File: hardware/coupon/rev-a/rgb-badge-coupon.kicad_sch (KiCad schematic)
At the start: 0 parts

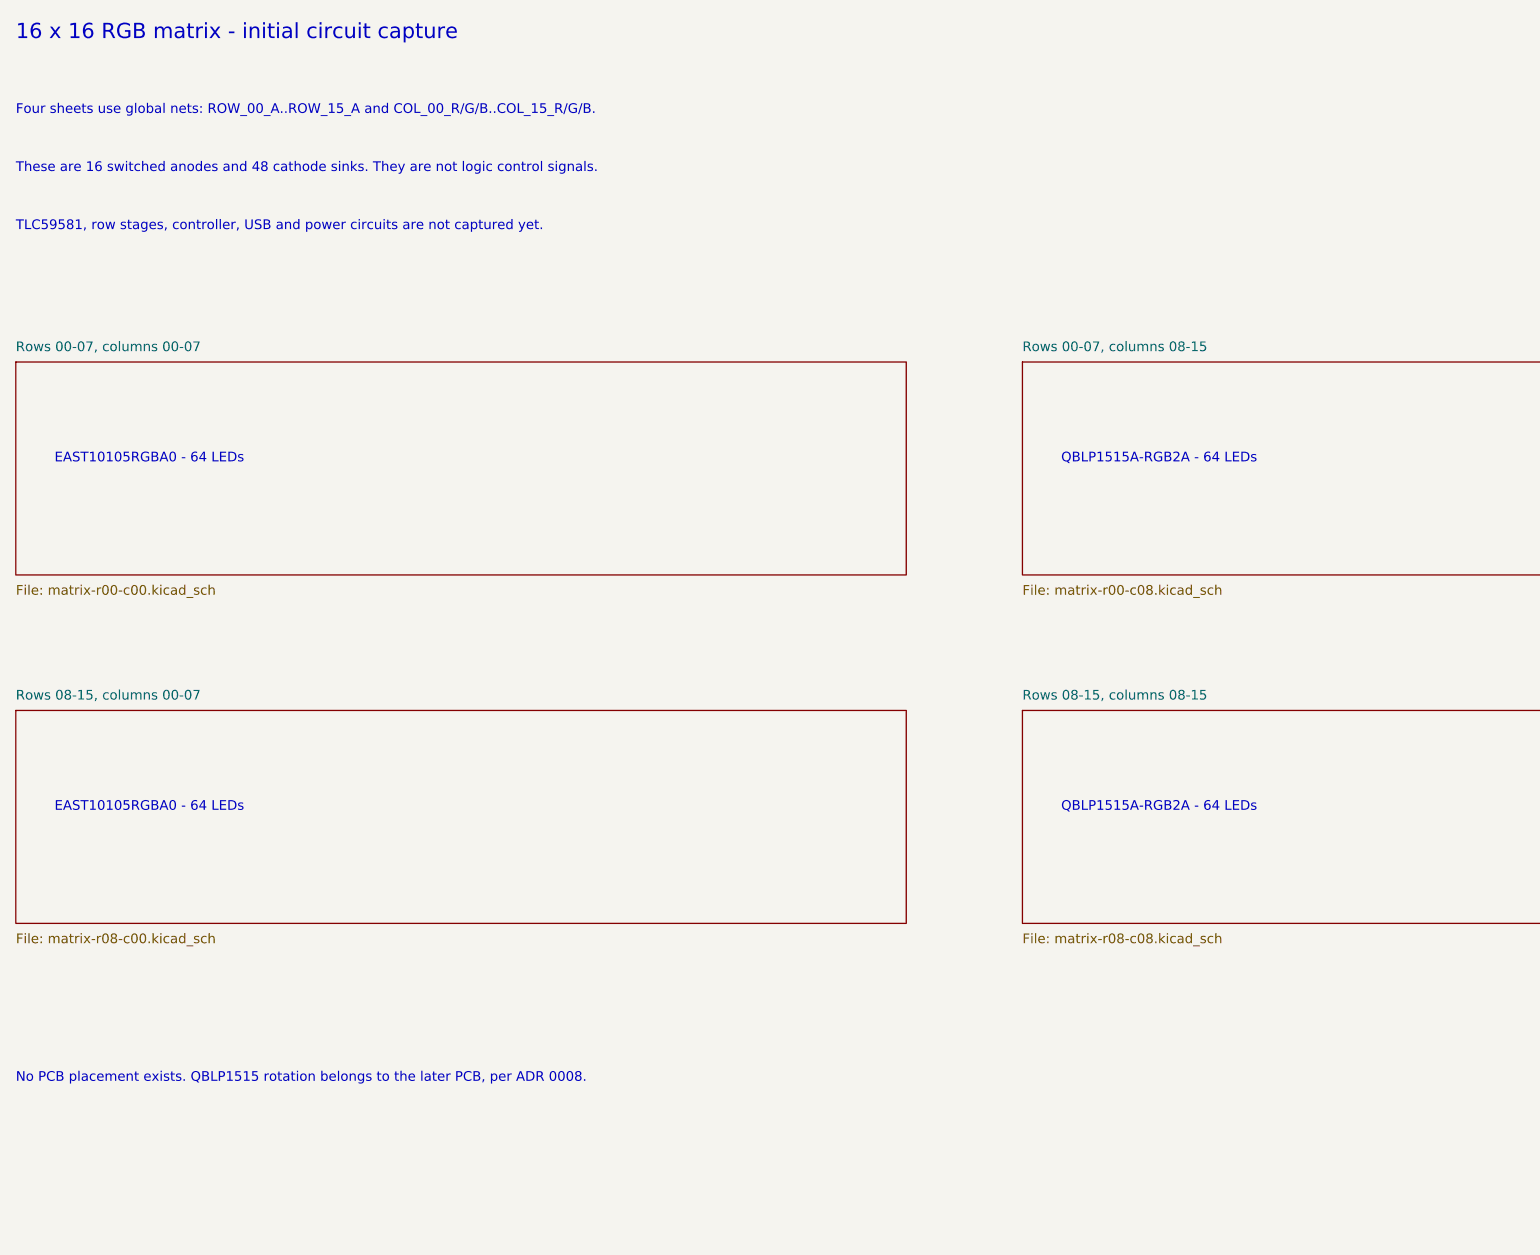
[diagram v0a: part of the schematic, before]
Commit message: Capture TLC59581 coupon driver and audit its current reference and footprint
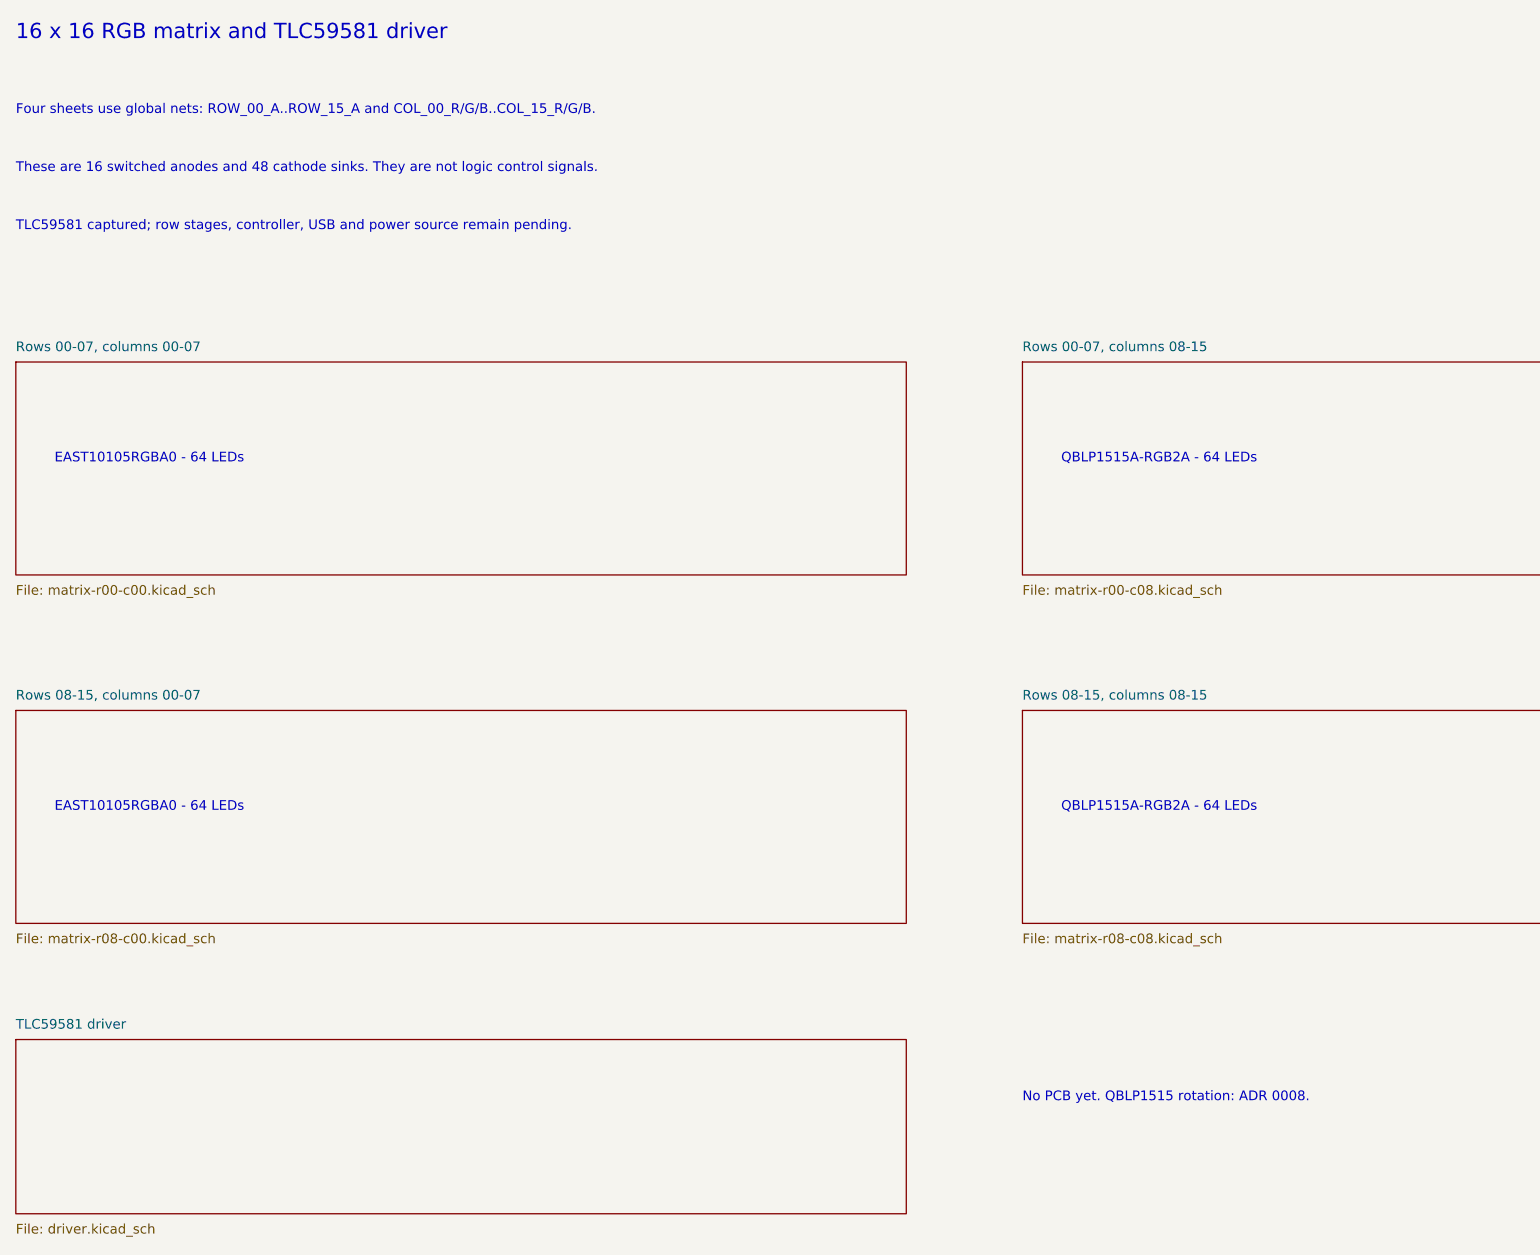
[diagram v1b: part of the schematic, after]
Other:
- added sheet TLC59581 driver (driver.kicad_sch)
- note added: "16 x 16 RGB matrix and TLC59581 driver"
- note added: "No PCB yet. QBLP1515 rotation: ADR 0008."
- note added: "TLC59581 captured; row stages, controller, USB and power source remain pending."
- note removed: "16 x 16 RGB matrix - initial circuit capture"
- note removed: "No PCB placement exists. QBLP1515 rotation belongs to the later PCB, per ADR 0008."
- note removed: "TLC59581, row stages, controller, USB and power circuits are not captured yet."
- title: Coupon Rev A - matrix capture -> Coupon Rev A - matrix and driver
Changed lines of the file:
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@@
 (generator_version "1.0")
 (paper "A4")
-(title_block (title "Coupon Rev A - matrix capture") (rev "A-draft") (comment 1 "SPDX-License-Identifier: CERN-OHL-S-2.0") (comment 2 "Matrix only: driver, row stages and power circuits pending"))
-(text "16 x 16 RGB matrix - initial circuit capture" (at 20.32 20.32 0) (effects (font (size 2.0 2.0)) (justify left)))
+(title_block (title "Coupon Rev A - matrix and driver") (rev "A-draft") (comment 1 "SPDX-License-Identifier: CERN-OHL-S-2.0") (comment 2 "Matrix and driver: row stages, controller and power pending"))
+(text "16 x 16 RGB matrix and TLC59581 driver" (at 20.32 20.32 0) (effects (font (size 2.0 2.0)) (justify left)))
 (text "Four sheets use global nets: ROW_00_A..ROW_15_A and COL_00_R/G/B..COL_15_R/G/B." (at 20.32 30.48 0) (effects (font (size 1.27 1.27)) (justify left)))
 (text "These are 16 switched anodes and 48 cathode sinks. They are not logic control signals." (at 20.32 38.10 0) (effects (font (size 1.27 1.27)) (justify left)))
-(text "TLC59581, row stages, controller, USB and power circuits are not captured yet." (at 20.32 45.72 0) (effects (font (size 1.27 1.27)) (justify left)))
-(text "No PCB placement exists. QBLP1515 rotation belongs to the later PCB, per ADR 0008." (at 20.32 157.48 0) (effects (font (size 1.27 1.27)) (justify left)))
+(text "TLC59581 captured; row stages, controller, USB and power source remain pending." (at 20.32 45.72 0) (effects (font (size 1.27 1.27)) (justify left)))
+(text "No PCB yet. QBLP1515 rotation: ADR 0008." (at 152.40 160.02 0) (effects (font (size 1.27 1.27)) (justify left)))
 (sheet (at 20.32 63.50) (size 116.84 27.94)
 (exclude_from_sim no) (in_bom yes) (on_board yes) (dnp no)
@@
 (instances (project "rgb-badge-coupon" (path "/207fb68e-2ddb-46bb-8712-eba2f8c5eef6" (page "5")))))
 (text "QBLP1515A-RGB2A - 64 LEDs" (at 157.48 121.92 0) (effects (font (size 1.27 1.27)) (justify left)))
+(sheet (at 20.32 152.40) (size 116.84 22.86)
+(exclude_from_sim no) (in_bom yes) (on_board yes) (dnp no)
+(stroke (width 0.1524) (type solid)) (fill (color 0 0 0 0))
+(property "Sheetname" "TLC59581 driver" (at 20.32 151.13 0) (effects (font (size 1.27 1.27)) (justify left bottom)))
+(property "Sheetfile" "driver.kicad_sch" (at 20.32 176.53 0) (effects (font (size 1.27 1.27)) (justify left top)))
+(instances (project "rgb-badge-coupon" (path "/207fb68e-2ddb-46bb-8712-eba2f8c5eef6" (page "6")))))
 (sheet_instances (path "/" (page "1")))
 (embedded_fonts no)

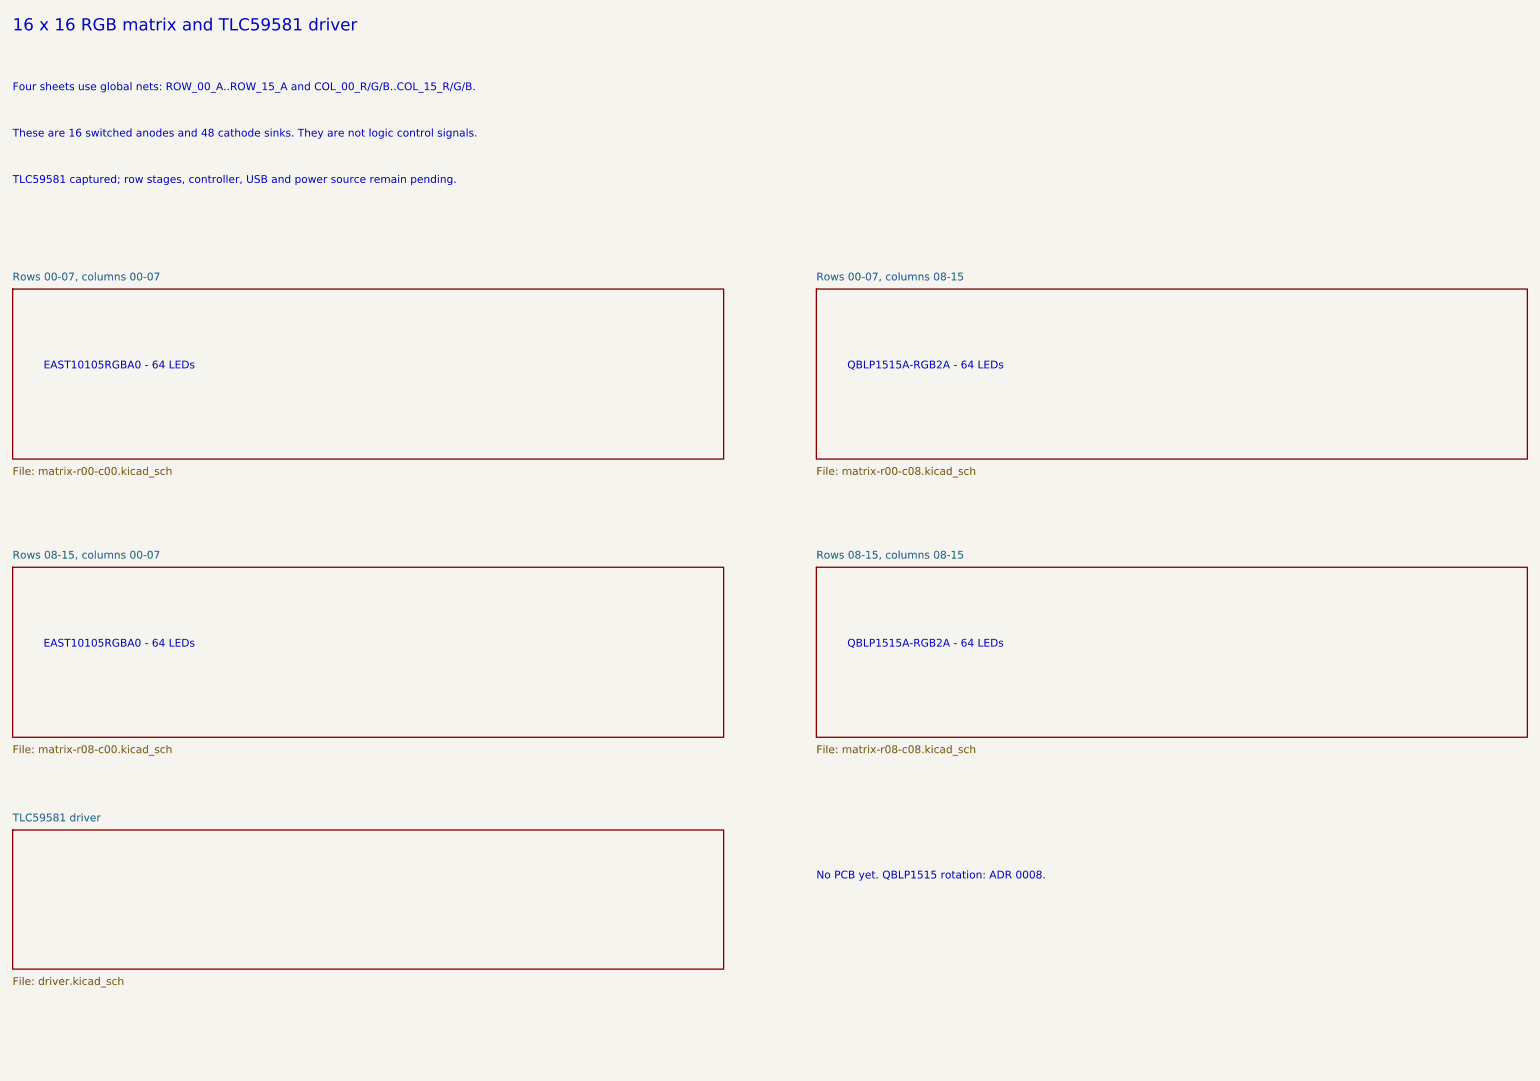
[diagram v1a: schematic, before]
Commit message: Capture Coupon Rev A row selectors
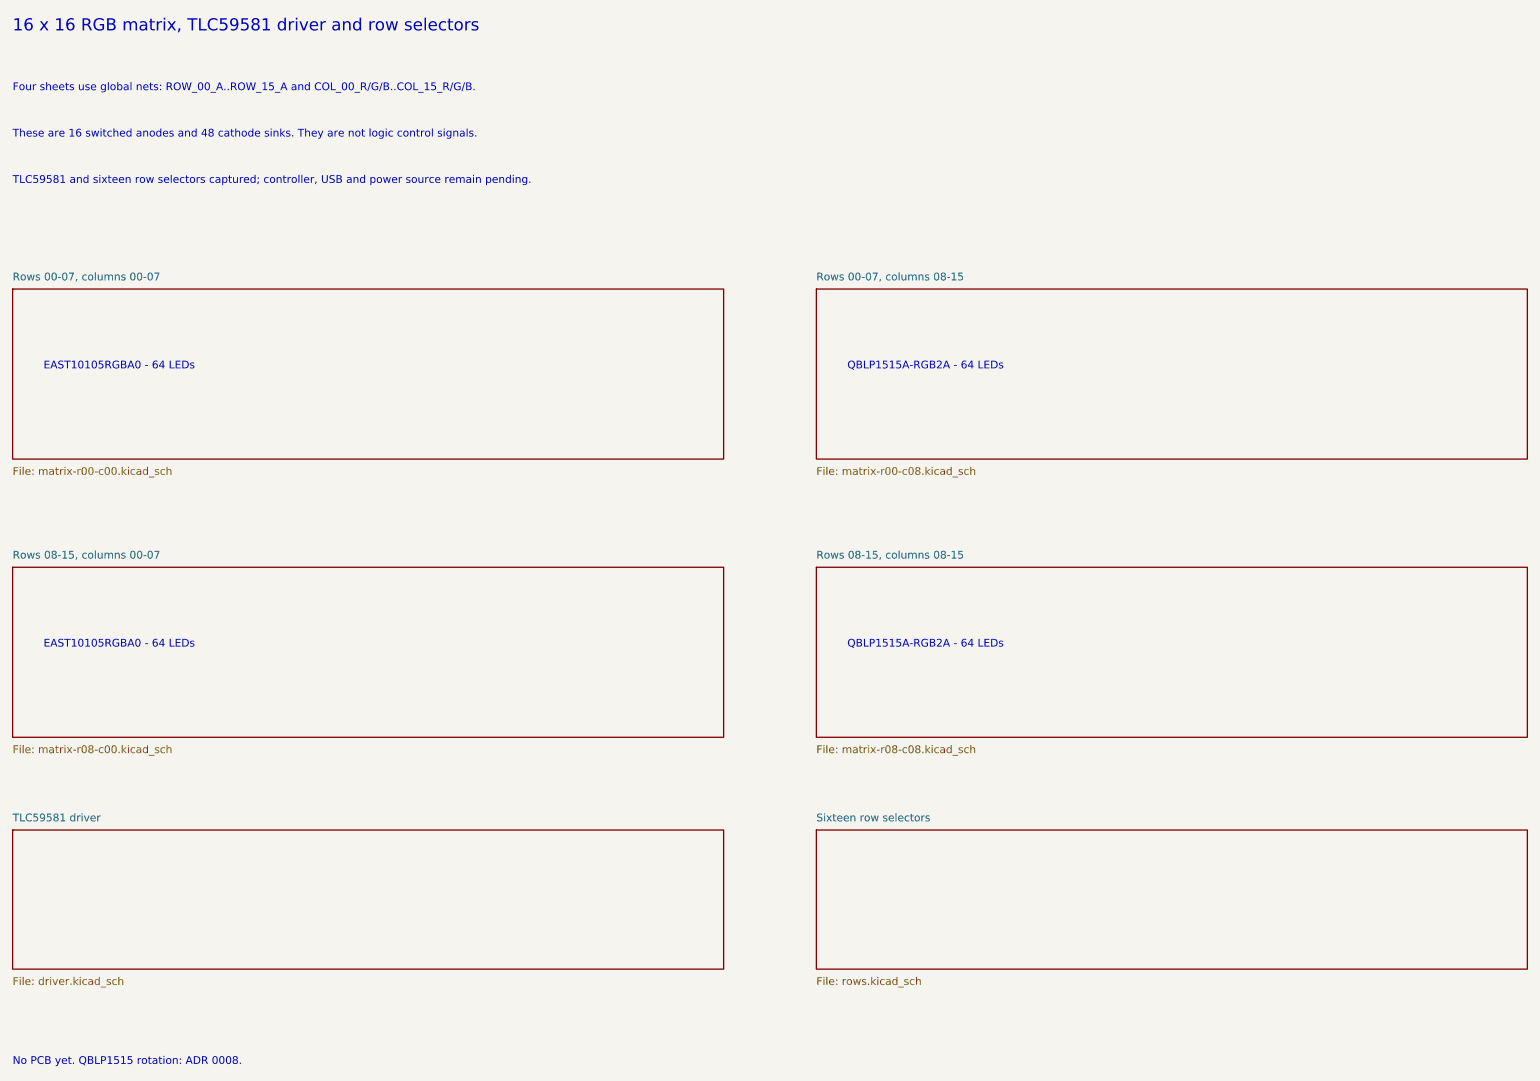
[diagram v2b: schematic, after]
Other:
- added sheet Sixteen row selectors (rows.kicad_sch)
- note added: "16 x 16 RGB matrix, TLC59581 driver and row selectors"
- note added: "TLC59581 and sixteen row selectors captured; controller, USB and power source remain pending."
- note removed: "16 x 16 RGB matrix and TLC59581 driver"
- note removed: "TLC59581 captured; row stages, controller, USB and power source remain pending."
- title: Coupon Rev A - matrix and driver -> Coupon Rev A - matrix, driver and rows
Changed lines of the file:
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@@
 (generator_version "1.0")
 (paper "A4")
-(title_block (title "Coupon Rev A - matrix and driver") (rev "A-draft") (comment 1 "SPDX-License-Identifier: CERN-OHL-S-2.0") (comment 2 "Matrix and driver: row stages, controller and power pending"))
-(text "16 x 16 RGB matrix and TLC59581 driver" (at 20.32 20.32 0) (effects (font (size 2.0 2.0)) (justify left)))
+(title_block (title "Coupon Rev A - matrix, driver and rows") (rev "A-draft") (comment 1 "SPDX-License-Identifier: CERN-OHL-S-2.0") (comment 2 "Controller and power circuits pending"))
+(text "16 x 16 RGB matrix, TLC59581 driver and row selectors" (at 20.32 20.32 0) (effects (font (size 2.0 2.0)) (justify left)))
 (text "Four sheets use global nets: ROW_00_A..ROW_15_A and COL_00_R/G/B..COL_15_R/G/B." (at 20.32 30.48 0) (effects (font (size 1.27 1.27)) (justify left)))
 (text "These are 16 switched anodes and 48 cathode sinks. They are not logic control signals." (at 20.32 38.10 0) (effects (font (size 1.27 1.27)) (justify left)))
-(text "TLC59581 captured; row stages, controller, USB and power source remain pending." (at 20.32 45.72 0) (effects (font (size 1.27 1.27)) (justify left)))
-(text "No PCB yet. QBLP1515 rotation: ADR 0008." (at 152.40 160.02 0) (effects (font (size 1.27 1.27)) (justify left)))
+(text "TLC59581 and sixteen row selectors captured; controller, USB and power source remain pending." (at 20.32 45.72 0) (effects (font (size 1.27 1.27)) (justify left)))
+(text "No PCB yet. QBLP1515 rotation: ADR 0008." (at 20.32 190.50 0) (effects (font (size 1.27 1.27)) (justify left)))
 (sheet (at 20.32 63.50) (size 116.84 27.94)
 (exclude_from_sim no) (in_bom yes) (on_board yes) (dnp no)
@@
 (property "Sheetfile" "driver.kicad_sch" (at 20.32 176.53 0) (effects (font (size 1.27 1.27)) (justify left top)))
 (instances (project "rgb-badge-coupon" (path "/207fb68e-2ddb-46bb-8712-eba2f8c5eef6" (page "6")))))
+(sheet (at 152.40 152.40) (size 116.84 22.86)
+(exclude_from_sim no) (in_bom yes) (on_board yes) (dnp no)
+(stroke (width 0.1524) (type solid)) (fill (color 0 0 0 0))
+(property "Sheetname" "Sixteen row selectors" (at 152.40 151.13 0) (effects (font (size 1.27 1.27)) (justify left bottom)))
+(property "Sheetfile" "rows.kicad_sch" (at 152.40 176.53 0) (effects (font (size 1.27 1.27)) (justify left top)))
+(instances (project "rgb-badge-coupon" (path "/207fb68e-2ddb-46bb-8712-eba2f8c5eef6" (page "7")))))
 (sheet_instances (path "/" (page "1")))
 (embedded_fonts no)
